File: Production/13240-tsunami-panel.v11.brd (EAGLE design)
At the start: 247.1 x 161.5 mm, 939 parts, among them J1 VDC-IN, J10 TRIG2, J11 TRIG1, J12 USD-SDIO-SOCKET, J13 GND, J14 AUDIO I/O, J15 MIDI, J16 USB-MICROB", J17 AUDIO I/O, J18 USD-SDIO-SOCKET, J19 CORTEX_DEBUGPTH, J2 GND-IN, J20 3.3VA, J21 3.3V, J22 FTDI_DEVICE, J23 TRIG2, J24 TRIG1, J25 GND, J26 MIDI, J27 DEBUG, J28 PLAYING, J29 VDC-IN, J3 DEBUG, J30 GND-IN, J31 USB-MICROB", J32 AUDIO I/O, J33 USD-SDIO-SOCKET, J34 CORTEX_DEBUGPTH, J35 3.3VA, J36 3.3V, J37 FTDI_DEVICE, J38 TRIG2, J39 TRIG1, J4 USB-MICROB", J40 GND, J41 MIDI, J42 DEBUG, J43 PLAYING, J44 VDC-IN, J45 GND-IN, J46 USB-MICROB", J47 AUDIO I/O, J48 USD-SDIO-SOCKET, J49 CORTEX_DEBUGPTH, J5 CORTEX_DEBUGPTH, J50 3.3VA, J51 3.3V, J52 FTDI_DEVICE, J53 TRIG2, J54 TRIG1, J55 GND, J56 MIDI, J57 DEBUG, J58 PLAYING, J59 VDC-IN, J6 3.3VA, J60 GND-IN, J61 USB-MICROB", J62 AUDIO I/O, J63 USD-SDIO-SOCKET, J64 CORTEX_DEBUGPTH, J65 3.3VA, J66 3.3V, J67 FTDI_DEVICE, J68 TRIG2, J69 TRIG1, J7 3.3V, J70 GND, J71 MIDI, J72 DEBUG, J73 PLAYING, J74 VDC-IN, J75 GND-IN, J76 USB-MICROB", J77 AUDIO I/O, J78 USD-SDIO-SOCKET, J79 CORTEX_DEBUGPTH, J8 PLAYING, J80 3.3VA, J81 3.3V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

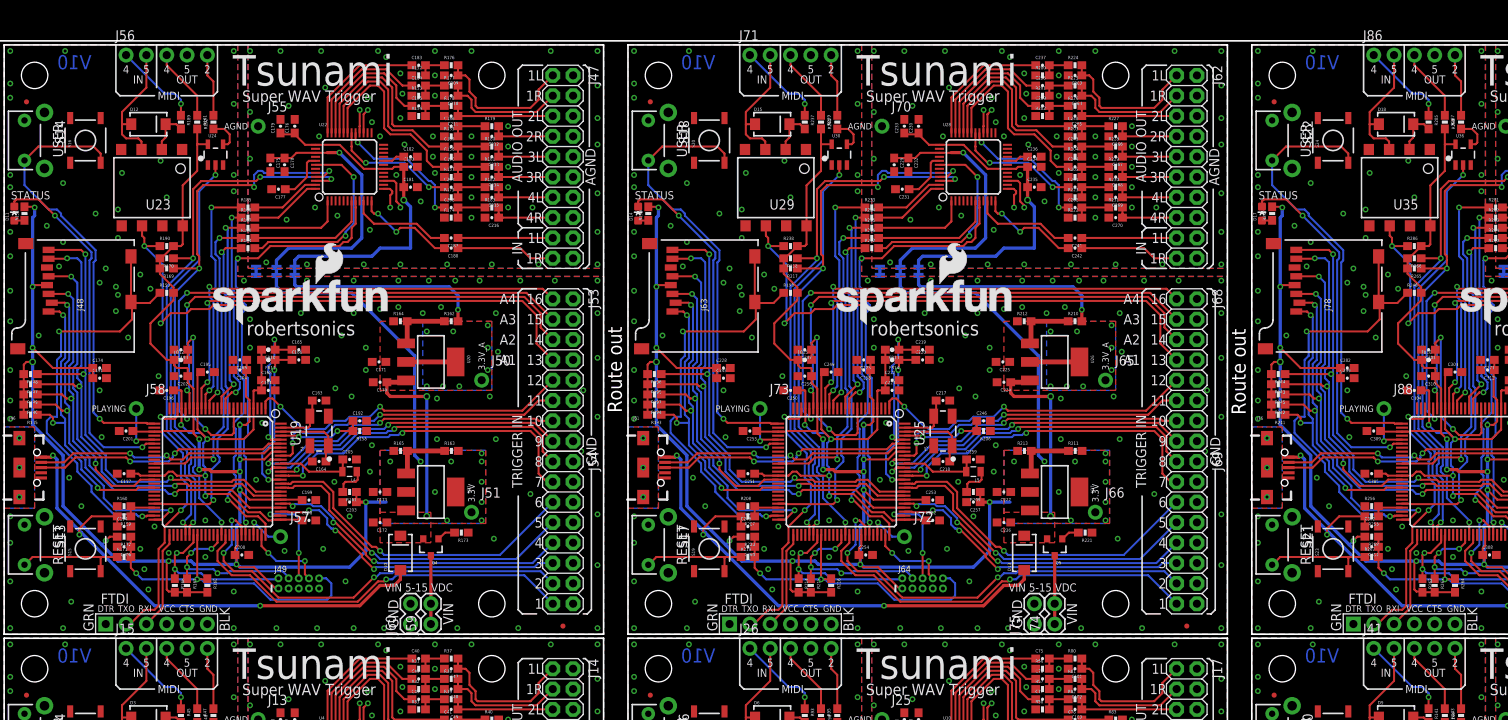
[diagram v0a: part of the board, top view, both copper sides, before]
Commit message: Fixing silkscreen labels on panel.
Transposed 2 and 5 labels on MIDI out port.
Rolled version to V11 on all files.
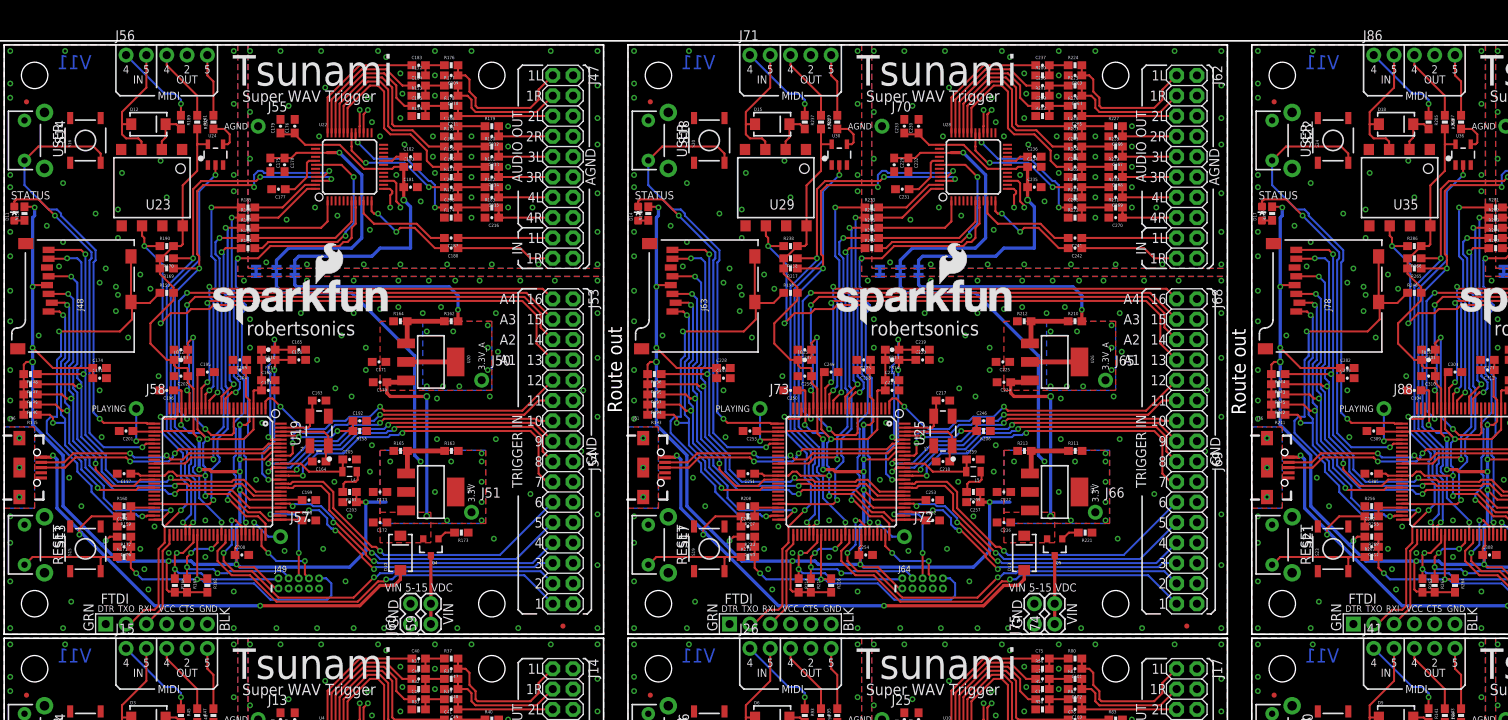
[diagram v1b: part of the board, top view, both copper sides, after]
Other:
- board text added: "V11"
- board text removed: "V10"
